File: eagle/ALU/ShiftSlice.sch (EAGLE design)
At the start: 0 parts

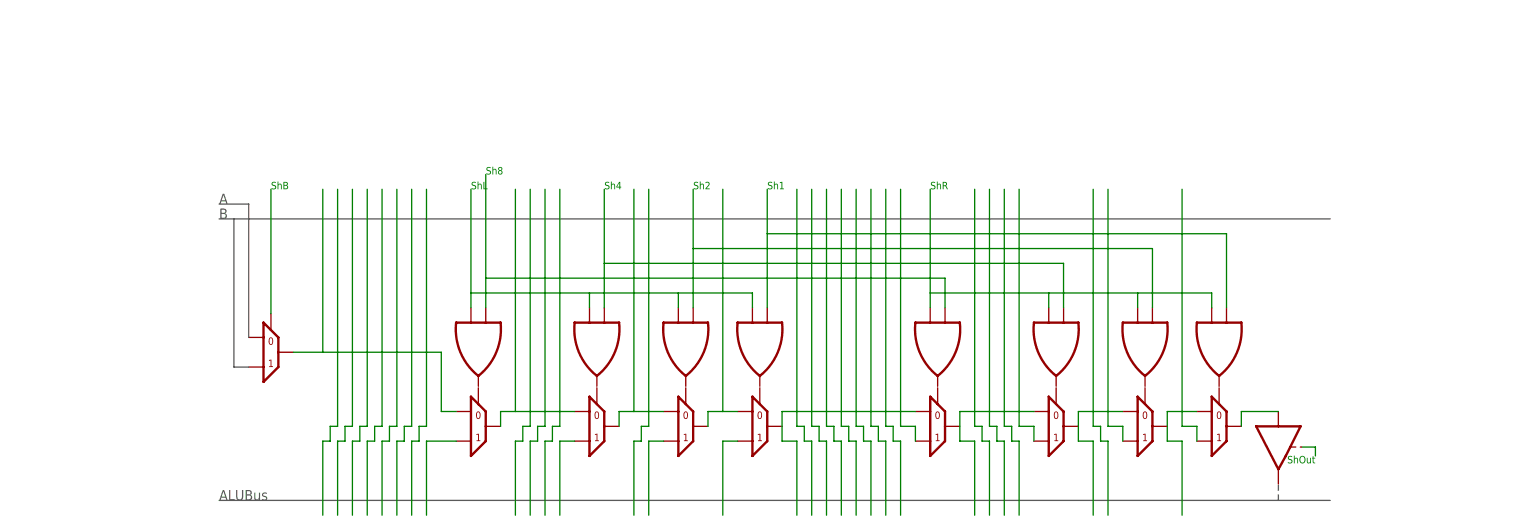
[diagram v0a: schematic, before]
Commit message: Eagle schematics now use library
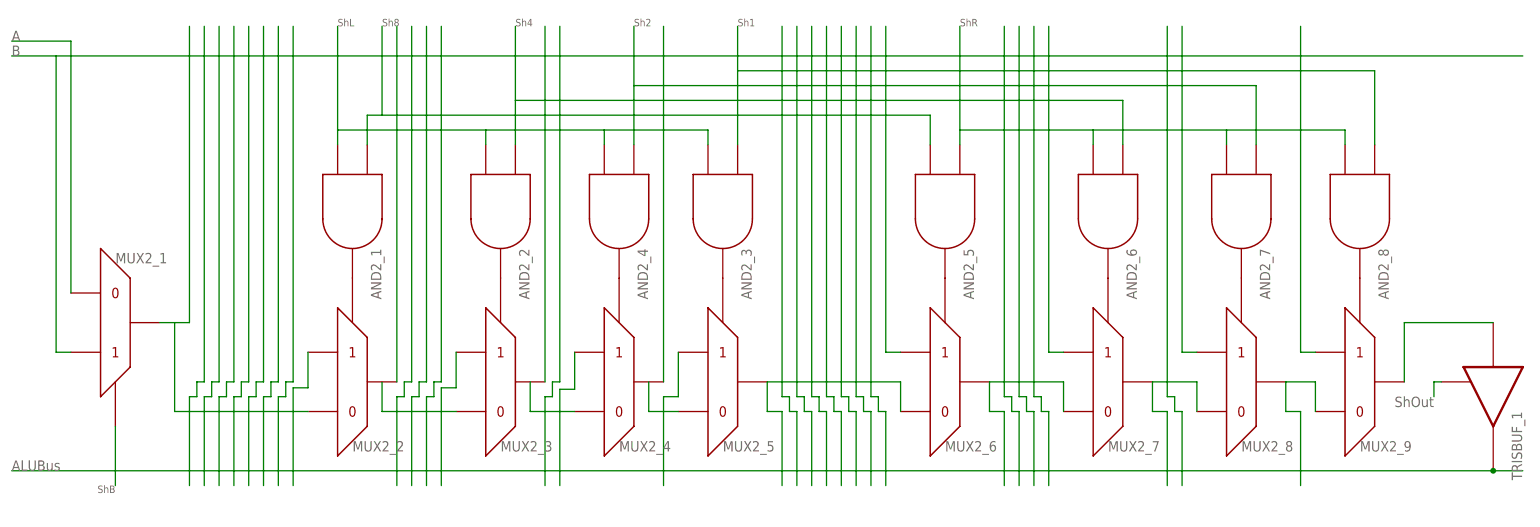
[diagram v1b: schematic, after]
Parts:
- added AND2_1, AND2_2, AND2_3, AND2_4, AND2_5, AND2_6, AND2_7, AND2_8: AND2, c035u:AND2
- added MUX2_1, MUX2_2, MUX2_3, MUX2_4, MUX2_5, MUX2_6, MUX2_7, MUX2_8, MUX2_9: MUX2, c035u:MUX2
- added TRISBUF_1: TRISBUF, c035u:TRISBUF
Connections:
- new net N$1: AND2_1.I1, AND2_2.I1, AND2_3.I1, AND2_4.I1
- new net N$10: MUX2_2.P$2
- new net N$18: MUX2_1.P$3, MUX2_2.P$1
- new net N$2: AND2_5.A, AND2_6.I1, AND2_7.I1, AND2_8.I1
- new net N$23: MUX2_3.P$2
- new net N$24: MUX2_4.P$2
- new net N$25: MUX2_5.P$2
- new net N$27: MUX2_6.P$2
- new net N$3: MUX2_2.P$3
- new net N$37: MUX2_7.P$2
- new net N$39: MUX2_8.P$2
- new net N$4: MUX2_3.P$3
- new net N$40: MUX2_9.P$2
- new net N$41: AND2_1.A, AND2_5.I1
- new net N$42: AND2_2.A, AND2_6.A
- new net N$43: AND2_4.A, AND2_7.A
- new net N$44: AND2_3.A, AND2_8.A
- new net N$45: MUX2_1.P$4
- new net N$46: MUX2_4.P$1
- new net N$47: MUX2_9.P$3, TRISBUF_1.I
- new net N$48: TRISBUF_1.P$1
- new net N$49: MUX2_1.P$1
- new net N$5: MUX2_4.P$3
- new net N$50: MUX2_1.P$2
- new net N$52: AND2_1.O, MUX2_2.P$4
- new net N$53: AND2_2.O, MUX2_3.P$4
- new net N$54: AND2_4.O, MUX2_4.P$4
- new net N$55: AND2_3.O, MUX2_5.P$4
- new net N$56: AND2_5.O, MUX2_6.P$4
- new net N$57: AND2_6.O, MUX2_7.P$4
- new net N$58: AND2_7.O, MUX2_8.P$4
- new net N$59: AND2_8.O, MUX2_9.P$4
- new net N$6: MUX2_6.P$3, MUX2_7.P$1
- new net N$60: TRISBUF_1.O
- new net N$61: MUX2_5.P$1
- new net N$62: MUX2_3.P$1
- new net N$63: MUX2_5.P$3, MUX2_6.P$1
- new net N$8: MUX2_7.P$3, MUX2_8.P$1
- new net N$9: MUX2_8.P$3, MUX2_9.P$1
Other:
- note removed: "0"
- note removed: "1"

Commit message: Schematics small improvements
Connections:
- removed net N$48: TRISBUF_1.P$1
- removed net N$60: TRISBUF_1.O
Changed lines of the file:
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@@
 <text x="-73.66" y="149.86" size="1.778" layer="95">B</text>
 <text x="-73.66" y="78.74" size="1.778" layer="95">ALUBus</text>
-<text x="-17.78" y="154.94" size="1.27" layer="95">ShL</text>
-<text x="88.9" y="154.94" size="1.27" layer="95">ShR</text>
-<text x="-10.16" y="154.94" size="1.27" layer="95">Sh8</text>
-<text x="12.7" y="154.94" size="1.27" layer="95">Sh4</text>
-<text x="33.02" y="154.94" size="1.27" layer="95">Sh2</text>
-<text x="50.8" y="154.94" size="1.27" layer="95">Sh1</text>
-<text x="-55.88" y="76.2" size="1.27" layer="95" rot="R180">ShB</text>
+<text x="-17.78" y="154.94" size="1.6764" layer="95">ShL</text>
+<text x="88.9" y="154.94" size="1.6764" layer="95">ShR</text>
+<text x="-10.16" y="154.94" size="1.6764" layer="95">Sh8</text>
+<text x="12.7" y="154.94" size="1.6764" layer="95">Sh4</text>
+<text x="33.02" y="154.94" size="1.6764" layer="95">Sh2</text>
+<text x="50.8" y="154.94" size="1.6764" layer="95">Sh1</text>
+<text x="-55.88" y="76.2" size="1.6764" layer="95" rot="R180">ShB</text>
 <wire x1="-76.2" y1="154.94" x2="-48.26" y2="154.94" width="0.1524" layer="98" style="longdash"/>
 <wire x1="-48.26" y1="154.94" x2="-48.26" y2="73.66" width="0.1524" layer="98" style="longdash"/>
 <wire x1="-48.26" y1="73.66" x2="-76.2" y2="73.66" width="0.1524" layer="98" style="longdash"/>
 <wire x1="-76.2" y1="73.66" x2="-76.2" y2="154.94" width="0.1524" layer="98" style="longdash"/>
-<text x="-74.422" y="74.168" size="1.27" layer="98">LUI</text>
-<text x="170.18" y="91.44" size="1.778" layer="95" font="vector" rot="R180">ShOut</text>
+<text x="-74.422" y="74.168" size="1.6764" layer="98">LUI</text>
+<text x="175.26" y="93.98" size="1.6764" layer="95" font="vector" rot="R180">ShOut</text>
 </plain>
 <instances>
@@
 </instances>
 <busses>
+<bus name="B$1">
+<segment>
+<wire x1="-73.66" y1="78.74" x2="185.42" y2="78.74" width="0.1524" layer="92"/>
+</segment>
+</bus>
 </busses>
 <nets>
@@
 <pinref part="AND2_3" gate="G$1" pin="I1"/>
 <wire x1="45.72" y1="134.62" x2="45.72" y2="137.16" width="0.1524" layer="91"/>
+<junction x="-17.78" y="137.16"/>
+<junction x="7.62" y="137.16"/>
+<junction x="27.94" y="137.16"/>
 </segment>
 </net>
@@
 <pinref part="AND2_8" gate="G$1" pin="I1"/>
 <wire x1="154.94" y1="134.62" x2="154.94" y2="137.16" width="0.1524" layer="91"/>
+<junction x="88.9" y="137.16"/>
+<junction x="111.76" y="137.16"/>
+<junction x="134.62" y="137.16"/>
 </segment>
 </net>
@@
 <pinref part="MUX2_7" gate="G$1" pin="P$3"/>
 <wire x1="121.92" y1="88.9" x2="121.92" y2="93.98" width="0.1524" layer="91"/>
+<junction x="121.92" y="93.98"/>
 </segment>
 </net>
@@
 <wire x1="-45.72" y1="104.14" x2="-48.26" y2="104.14" width="0.1524" layer="91"/>
 <wire x1="-45.72" y1="88.9" x2="-45.72" y2="104.14" width="0.1524" layer="91"/>
+<junction x="-45.72" y="104.14"/>
 </segment>
 </net>
@@
 <pinref part="MUX2_8" gate="G$1" pin="P$3"/>
 <wire x1="144.78" y1="88.9" x2="144.78" y2="93.98" width="0.1524" layer="91"/>
+<junction x="144.78" y="93.98"/>
 </segment>
 </net>
@@
 <pinref part="AND2_1" gate="G$1" pin="A"/>
 <pinref part="AND2_5" gate="G$1" pin="I1"/>
+<junction x="-10.16" y="139.7"/>
 </segment>
 </net>
@@
 <pinref part="AND2_2" gate="G$1" pin="A"/>
 <pinref part="AND2_6" gate="G$1" pin="A"/>
+<junction x="12.7" y="142.24"/>
 </segment>
 </net>
@@
 <pinref part="AND2_4" gate="G$1" pin="A"/>
 <pinref part="AND2_7" gate="G$1" pin="A"/>
+<junction x="33.02" y="144.78"/>
 </segment>
 </net>
@@
 <pinref part="AND2_3" gate="G$1" pin="A"/>
 <pinref part="AND2_8" gate="G$1" pin="A"/>
+<junction x="50.8" y="147.32"/>
 </segment>
 </net>
@@
 <wire x1="-63.5" y1="99.06" x2="-66.04" y2="99.06" width="0.1524" layer="91"/>
 <wire x1="-66.04" y1="99.06" x2="-66.04" y2="149.86" width="0.1524" layer="91"/>
-</segment>
-</net>
-<net name="N$51" class="0">
-<segment>
-<wire x1="-73.66" y1="149.86" x2="185.42" y2="149.86" width="0.1524" layer="91"/>
+<wire x1="-73.66" y1="149.86" x2="-66.04" y2="149.86" width="0.1524" layer="91"/>
+<junction x="-66.04" y="149.86"/>
+<wire x1="-66.04" y1="149.86" x2="185.42" y2="149.86" width="0.1524" layer="91"/>
 </segment>
 </net>
@@
 </segment>
 </net>
-<net name="N$48" class="0">
-<segment>
-<pinref part="TRISBUF_1" gate="G$1" pin="P$1"/>
-<wire x1="171.45" y1="93.98" x2="170.18" y2="93.98" width="0.1524" layer="91"/>
-<wire x1="170.18" y1="93.98" x2="170.18" y2="91.44" width="0.1524" layer="91"/>
-</segment>
-</net>
-<net name="N$60" class="0">
-<segment>
-<wire x1="185.42" y1="78.74" x2="180.34" y2="78.74" width="0.1524" layer="91"/>
-<pinref part="TRISBUF_1" gate="G$1" pin="O"/>
-<wire x1="180.34" y1="78.74" x2="-73.66" y2="78.74" width="0.1524" layer="91"/>
-<junction x="180.34" y="78.74"/>
-</segment>
-</net>
 <net name="N$61" class="0">
 <segment>
@@
 <wire x1="40.64" y1="88.9" x2="35.56" y2="88.9" width="0.1524" layer="91"/>
 <wire x1="35.56" y1="88.9" x2="35.56" y2="93.98" width="0.1524" layer="91"/>
+<junction x="35.56" y="93.98"/>
 </segment>
 </net>
@@
 <wire x1="22.86" y1="88.9" x2="15.24" y2="88.9" width="0.1524" layer="91"/>
 <wire x1="15.24" y1="88.9" x2="15.24" y2="93.98" width="0.1524" layer="91"/>
+<junction x="15.24" y="93.98"/>
 </segment>
 </net>
@@
 <wire x1="2.54" y1="88.9" x2="-10.16" y2="88.9" width="0.1524" layer="91"/>
 <wire x1="-10.16" y1="88.9" x2="-10.16" y2="93.98" width="0.1524" layer="91"/>
+<junction x="-10.16" y="93.98"/>
 </segment>
 </net>
@@
 <pinref part="MUX2_5" gate="G$1" pin="P$3"/>
 <wire x1="55.88" y1="88.9" x2="55.88" y2="93.98" width="0.1524" layer="91"/>
+<junction x="55.88" y="93.98"/>
 </segment>
 </net>
@@
 <pinref part="MUX2_6" gate="G$1" pin="P$3"/>
 <wire x1="93.98" y1="88.9" x2="93.98" y2="93.98" width="0.1524" layer="91"/>
-</segment>
-</net>
+<junction x="93.98" y="93.98"/>
+</segment>
+</net>
